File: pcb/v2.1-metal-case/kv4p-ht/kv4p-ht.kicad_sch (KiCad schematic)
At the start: 67 parts, among them J1 Antenna, J5 USB-C Socket, Q1 SS8050, Q2 SS8050, Q3 AO3400A, SW3 Reset, SW4 Program, U1 DRA/SA818, U2 AZ1117H-3.3TRG1, U4 CP2102N-A02-GQFN24, U5 ESP32-WROOM-32E-N4

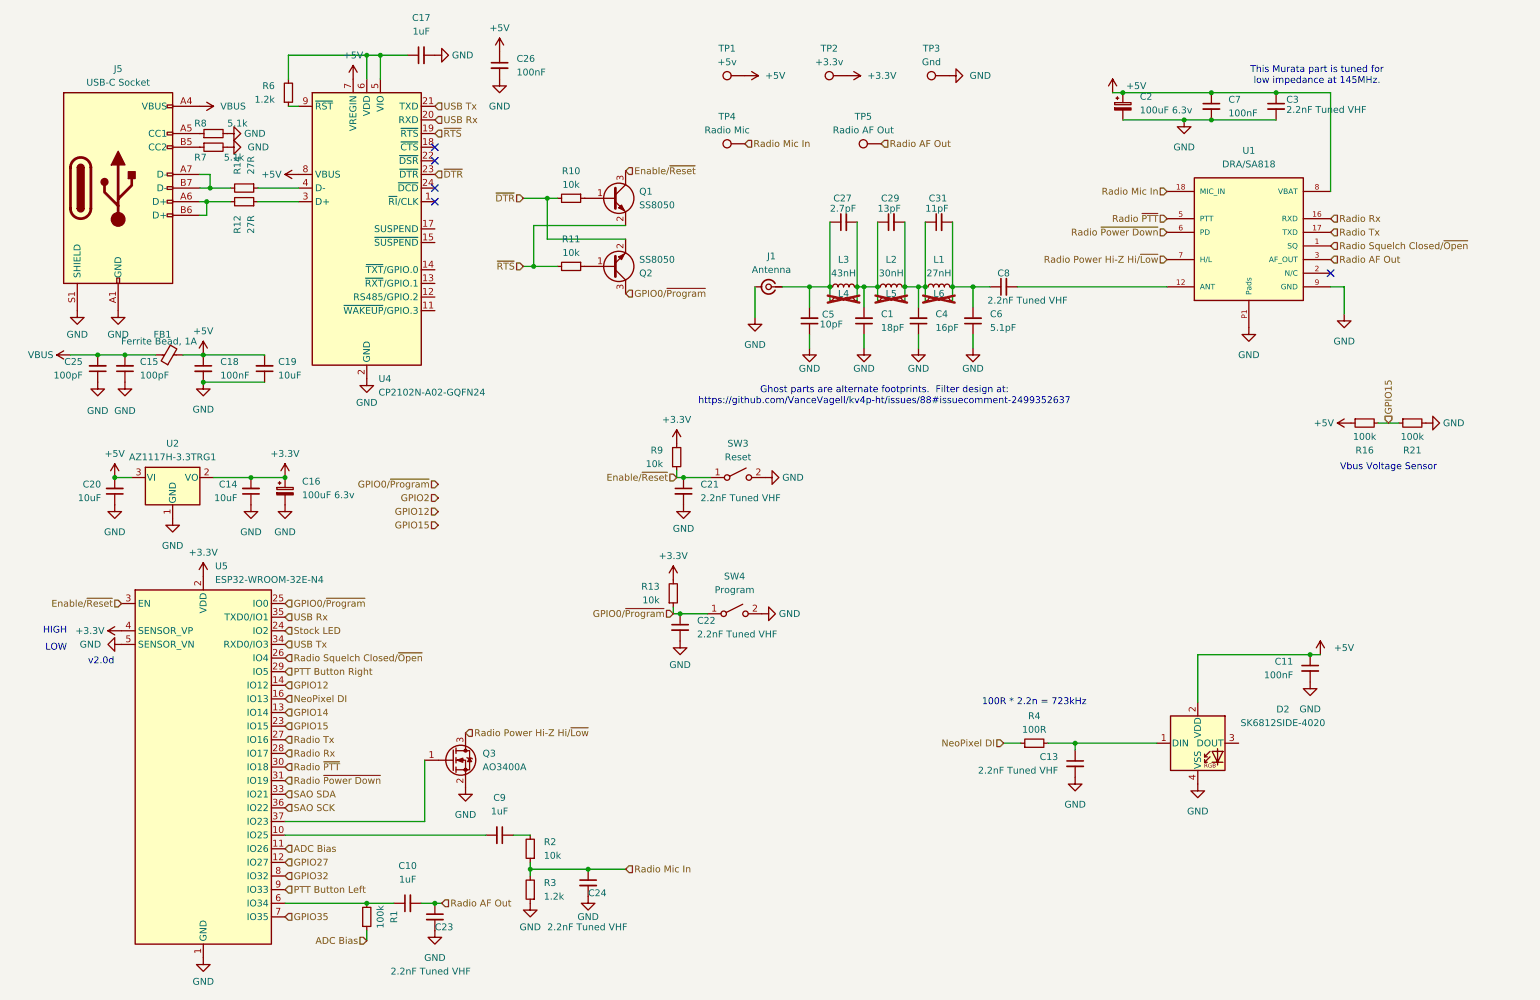
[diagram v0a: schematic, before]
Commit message: Working on a different case version of kv4p board.
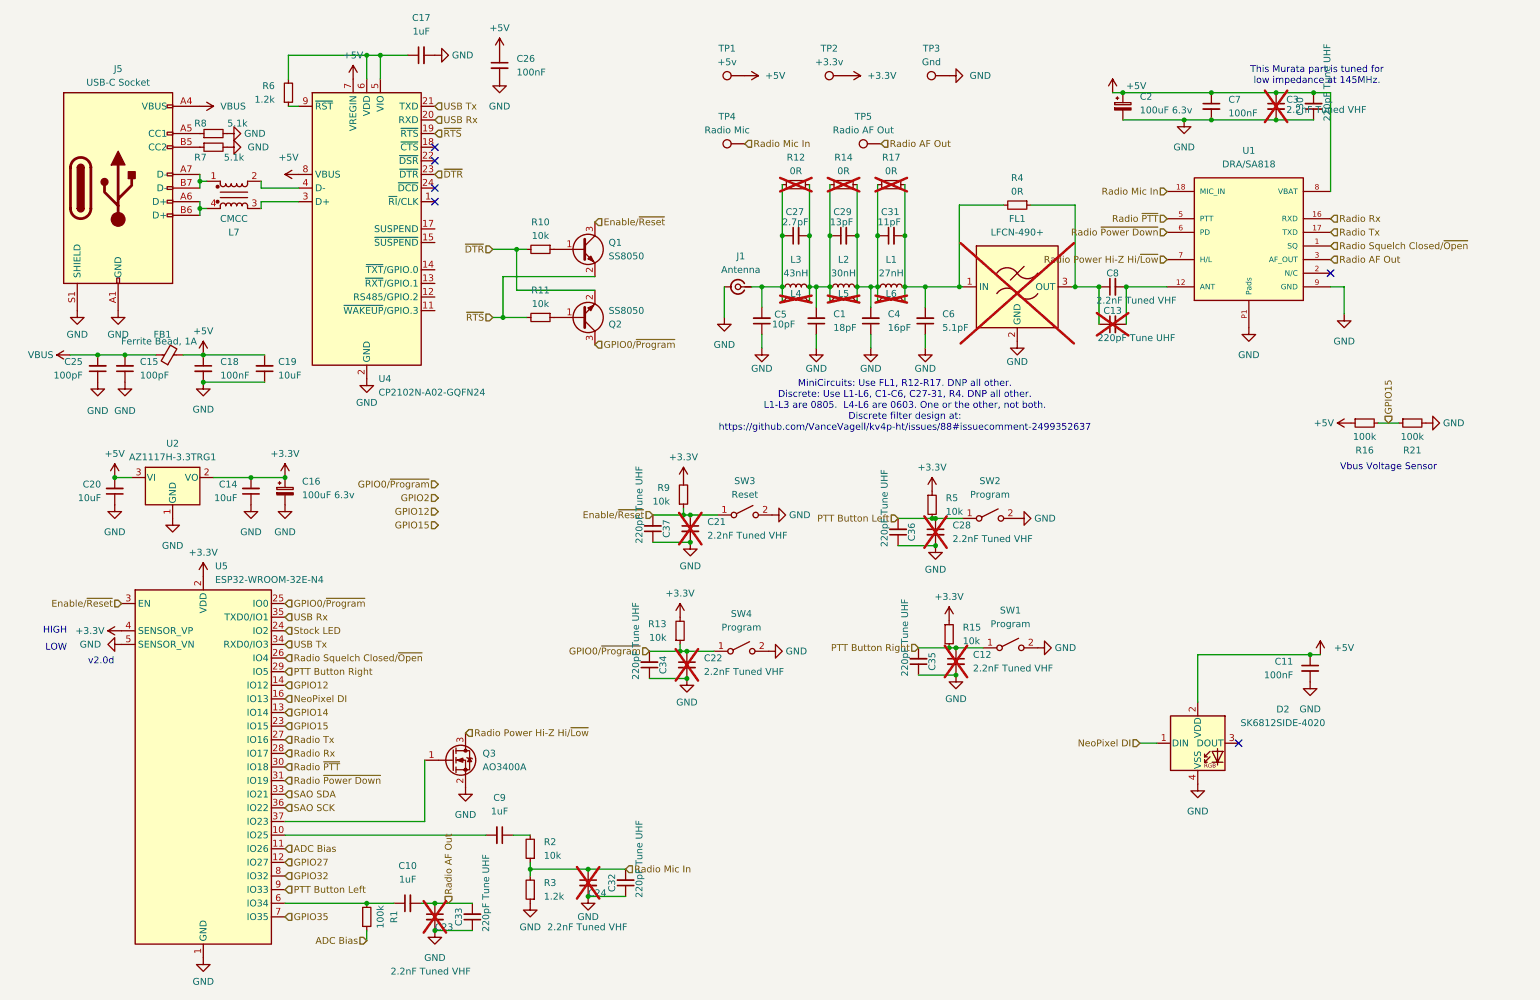
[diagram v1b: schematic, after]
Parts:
- added C12, C28: 2.2nF Tuned VHF, Capacitor_SMD:C_0603_1608Metric, symbol Device:C_Small
- added C30, C32, C33, C34, C35, C36, C37: 220pF Tune UHF, Capacitor_SMD:C_0603_1608Metric, symbol Device:C_Small
- added FL1: LFCN-490+, Filter:Filter_Mini-Circuits_FV1206, symbol RF_Filter:LFCN-160
- added L7: CMCC, Inductor_SMD:L_CommonMode_Wurth_WE-CNSW-1206, symbol Filter:Choke_Wurth_WE-CNSW_744232090
- added R15, R5: 10k, Resistor_SMD:R_0603_1608Metric, symbol Device:R_Small
- added R17: 0R, Resistor_SMD:R_0603_1608Metric, symbol Device:R_Small
- added SW1, SW2: Program, Button_Switch_SMD:SW_SPST_TL3342, symbol Switch:SW_SPST
- C13: value 2.2nF Tuned VHF -> 220pF Tune UHF; Alternate LCSC C882578, C2168957 -> (none); LCSC C2168957 -> C388907; Part Number GCM1885C1H222FA16D -> GCM1885C2A221JA16D; now not fitted
- C21, C22, C23, C24, C3: now not fitted
- R12, R14: value 27R -> 0R; LCSC C25190 -> C21189; now not fitted
- R4: value 100R -> 0R; footprint Resistor_SMD:R_0603_1608Metric -> Resistor_SMD:R_1206_3216Metric; LCSC C22775 -> C17888
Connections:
- net +3.3V: now also R15.1, R5.1
- net +5V: now also C30.2
- net Enable/~{Reset}: now also C37.2
- net GND: now also C12.2, C28.2, C30.1, C32.1, C33.1, C34.1, C35.1, C36.1, C37.1, FL1.2 (GND), FL1.4 (GND), SW1.2 (B), SW2.2 (B); no longer C13.2
- net GPIO0/~{Program}: now also C34.2
- net NeoPixel DI: now also D2.1 (DIN); no longer R4.1
- net PTT Button Left: now also C28.1, C36.2, R5.2, SW2.1 (A)
- net PTT Button Right: now also C12.1, C35.2, R15.2, SW1.1 (A)
- net Radio AF Out: now also C33.2
- net Radio Mic In: now also C32.2
- net at C27.1, C5.2, J1.1 (In)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: now also R12.2
- net at C1.2, C27.2, C29.1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: now also R12.1, R14.2
- net at U4.3 (D+): now also L7.3; no longer R12.1
- net at U4.4 (D-): now also L7.2; no longer R14.1
- net at C29.2, C31.1, C4.2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: now also R14.1, R17.2
- net at C31.2, C6.2, L1.2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: now also R4.2, FL1.1 (IN), R17.1; no longer C8.1
- net at C8.2, U1.12 (ANT): now also C13.2
- net at J5.A6 (D+), J5.B6 (D+): now also L7.4; no longer R12.2
- net at J5.A7 (D-), J5.B7 (D-): now also L7.1; no longer R14.2
- new net: C13.1, C8.1, FL1.3 (OUT), R4.1
- no-connect marks 5 -> 6
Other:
- note added: "MiniCircuits: Use FL1, R12-R17. DNP all other. Discrete: Use L1-L6, C1-C6, C27-31, R4. DNP all other. L1-L3 are 0805. L4-L6 are 0603. One or the other, not both. Discrete filter design at: https://github.com/VanceVagell/kv4p-ht/issues/88#issuecomment-2499352637"
- note removed: "100R * 2.2n = 723kHz"
- note removed: "Ghost parts are alternate footprints. Filter design at: https://github.com/VanceVagell/kv4p-ht/issues/88#issuecomment-2499352637"
- moved on the sheet: C1, C27, C29, C31, C4, C5, C6, C8, J1, L1, L2, L3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
